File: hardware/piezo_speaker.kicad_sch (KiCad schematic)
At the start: 4 parts, among them Q2 2N3904

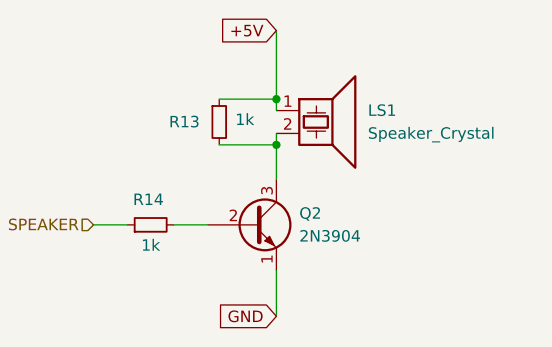
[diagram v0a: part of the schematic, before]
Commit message: Added information, footprints and 3d models for several components
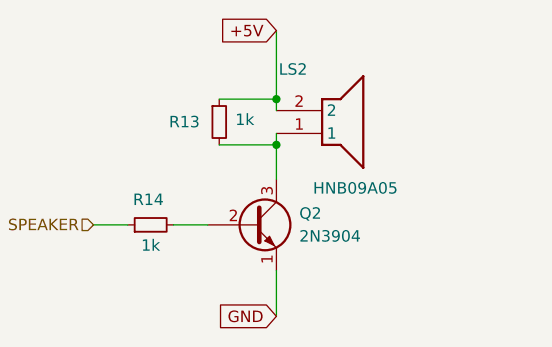
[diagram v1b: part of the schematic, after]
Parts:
- removed LS1: Speaker_Crystal, symbol Device:Speaker_Crystal
- added LS2: HNB09A05, HNB09A05, symbol kitchen_timer-symbols_lib:HNB09A05
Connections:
- net +5V: now also LS2.2
- net at Q2.3 (C), R13.2: now also LS2.1
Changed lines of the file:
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@@
+	)
+	(symbol
+		(lib_id "kitchen_timer-symbols_lib:HNB09A05")
+		(at 148.59 76.2 0)
+		(unit 1)
+		(exclude_from_sim no)
+		(in_bom yes)
+		(on_board yes)
+		(dnp no)
+		(property "Reference" "LS2"
+			(at 148.844 71.628 0)
+			(effects
+				(font
+					(size 1.27 1.27)
+				)
+				(justify left)
+			)
+		)
+		(property "Value" "HNB09A05"
+			(at 152.654 84.836 0)
+			(effects
+				(font
+					(size 1.27 1.27)
+				)
+				(justify left)
+			)
+		)
+		(property "Footprint" "HNB09A05"
+			(at 160.02 178.74 0)
+			(effects
+				(font
+					(size 1.27 1.27)
+				)
+				(justify left top)
+				(hide yes)
+			)
+		)
+		(property "Datasheet" "https://www.lcsc.com/datasheet/lcsc_datasheet_1811141138_Jiangsu-Huaneng-Elec-HNB09A05_C96493.pdf"
+			(at 160.02 278.74 0)
+			(effects
+				(font
+					(size 1.27 1.27)
+				)
+				(justify left top)
+				(hide yes)
+			)
+		)
+		(property "Description" "Buzzers Magnetic YES 3000+/-300Hz 5V 4 ~ 8V 9mm DIP RoHS"
+			(at 150.876 67.056 0)
+			(effects
+				(font
+					(size 1.27 1.27)
+				)
+				(hide yes)
+			)
+		)
+		(property "Height" "5.7"
+			(at 160.02 478.74 0)
+			(effects
+				(font
+					(size 1.27 1.27)
+				)
+				(justify left top)
+				(hide yes)
+			)
+		)
+		(property "Manufacturer_Name" "Jiangsu Huaneng Elec"
+			(at 160.02 578.74 0)
+			(effects
+				(font
+					(size 1.27 1.27)
+				)
+				(justify left top)
+				(hide yes)
+			)
+		)
+		(property "Manufacturer_Part_Number" "HNB09A05"
+			(at 160.02 678.74 0)
+			(effects
+				(font
+					(size 1.27 1.27)
+				)
+				(justify left top)
+				(hide yes)
+			)
+		)
+		(property "Mouser Part Number" ""
+			(at 160.02 778.74 0)
+			(effects
+				(font
+					(size 1.27 1.27)
+				)
+				(justify left top)
+				(hide yes)
+			)
+		)
+		(property "Mouser Price/Stock" ""
+			(at 160.02 878.74 0)
+			(effects
+				(font
+					(size 1.27 1.27)
+				)
+				(justify left top)
+				(hide yes)
+			)
+		)
+		(property "Arrow Part Number" ""
+			(at 160.02 978.74 0)
+			(effects
+				(font
+					(size 1.27 1.27)
+				)
+				(justify left top)
+				(hide yes)
+			)
+		)
+		(property "Arrow Price/Stock" ""
+			(at 160.02 1078.74 0)
+			(effects
+				(font
+					(size 1.27 1.27)
+				)
+				(justify left top)
+				(hide yes)
+			)
+		)
+		(property "Supplier Link" "https://jlcpcb.com/partdetail/Jiangsu_HuanengElec-HNB09A05/C96493"
+			(at 148.59 76.2 0)
+			(effects
+				(font
+					(size 1.27 1.27)
+				)
+				(hide yes)
+			)
+		)
+		(property "Price/unit" "$0.2261"
+			(at 148.59 76.2 0)
+			(effects
+				(font
+					(size 1.27 1.27)
+				)
+				(hide yes)
+			)
+		)
+		(property "Part Num" "HNB09A05"
+			(at 148.59 76.2 0)
+			(effects
+				(font
+					(size 1.27 1.27)
+				)
+				(hide yes)
+			)
+		)
+		(property "Package" "Plugin,D=9mm"
+			(at 148.59 76.2 0)
+			(effects
+				(font
+					(size 1.27 1.27)
+				)
+				(hide yes)
+			)
+		)
+		(pin "2"
+		)
+		(pin "1"
+		)
+		(instances
+			(project ""
+				(path "/8963deea-96bc-4401-b671-98fbe9ed9c6a/cc0cdeb4-aa65-40c1-8591-40f3174b886f"
+					(reference "LS2")
+					(unit 1)
+				)
+			)
+		)
 	)
 	(symbol
@@
 					(unit 1)
 				)
-			)
-		)
-	)
-	(symbol
-		(lib_id "Device:Speaker_Crystal")
-		(at 153.67 76.2 0)
-		(unit 1)
-		(exclude_from_sim no)
-		(in_bom yes)
-		(on_board yes)
-		(dnp no)
-		(fields_autoplaced yes)
-		(property "Reference" "LS1"
-			(at 158.75 76.1999 0)
-			(effects
-				(font
-					(size 1.27 1.27)
-				)
-				(justify left)
-			)
-		)
-		(property "Value" "Speaker_Crystal"
-			(at 158.75 78.7399 0)
-			(effects
-				(font
-					(size 1.27 1.27)
-				)
-				(justify left)
-			)
-		)
-		(property "Footprint" ""
-			(at 152.781 77.47 0)
-			(effects
-				(font
-					(size 1.27 1.27)
-				)
-				(hide yes)
-			)
-		)
-		(property "Datasheet" "~"
-			(at 152.781 77.47 0)
-			(effects
-				(font
-					(size 1.27 1.27)
-				)
-				(hide yes)
-			)
-		)
-		(property "Description" "Crystal speaker/transducer"
-			(at 153.67 76.2 0)
-			(effects
-				(font
-					(size 1.27 1.27)
-				)
-				(hide yes)
-			)
-		)
-		(pin "1"
-		)
-		(pin "2"
-		)
-		(instances
-			(project ""
-				(path "/8963deea-96bc-4401-b671-98fbe9ed9c6a/cc0cdeb4-aa65-40c1-8591-40f3174b886f"
-					(reference "LS1")
-					(unit 1)
-				)

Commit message: Added TP4056 footprint andconfirmed components in UART and BMS schematics.
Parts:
- LS2: footprint HNB09A05 -> kitchen_timer:HNB09A05
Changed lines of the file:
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@@
 			)
 		)
-		(property "Footprint" "HNB09A05"
+		(property "Footprint" "kitchen_timer:HNB09A05"
 			(at 160.02 178.74 0)
 			(effects

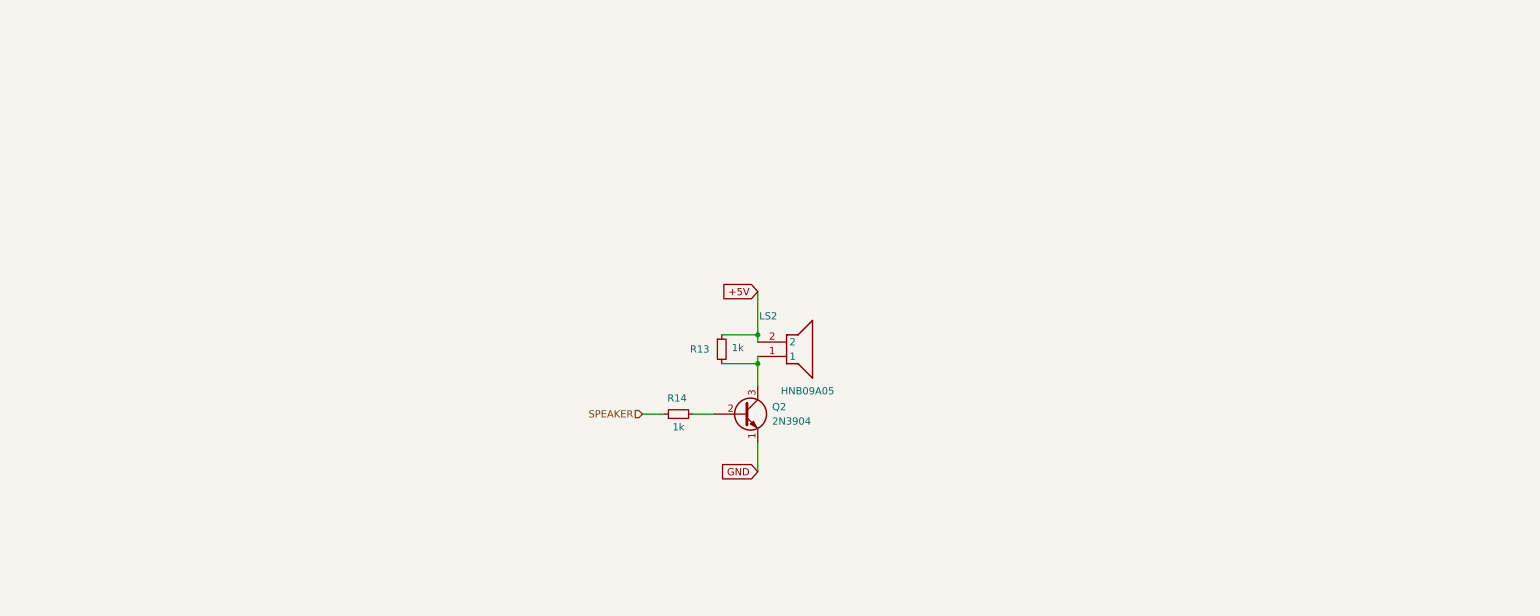
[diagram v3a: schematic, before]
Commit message: Schematic completed, commented and ready for review
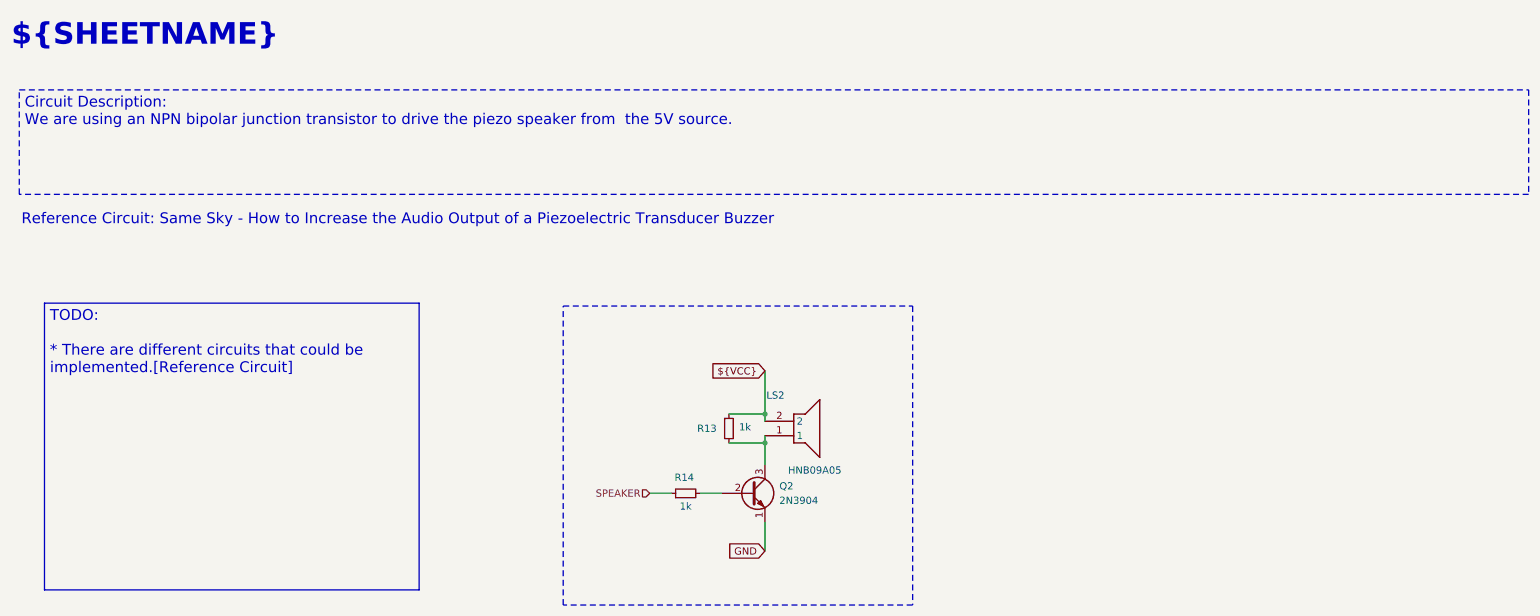
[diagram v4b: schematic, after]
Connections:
- net +5V renamed ${VCC}
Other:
- note added: "${SHEETNAME}"
- note added: "Reference Circuit: Same Sky - How to Increase the Audio Output of a Piezoelectric Transducer Buzzer"
- title: Kitchen_Timer - Piezo Speakr -> Kitchen_Timer - ${SHEETNAME}
- moved on the sheet: LS2, Q2, R13, R14

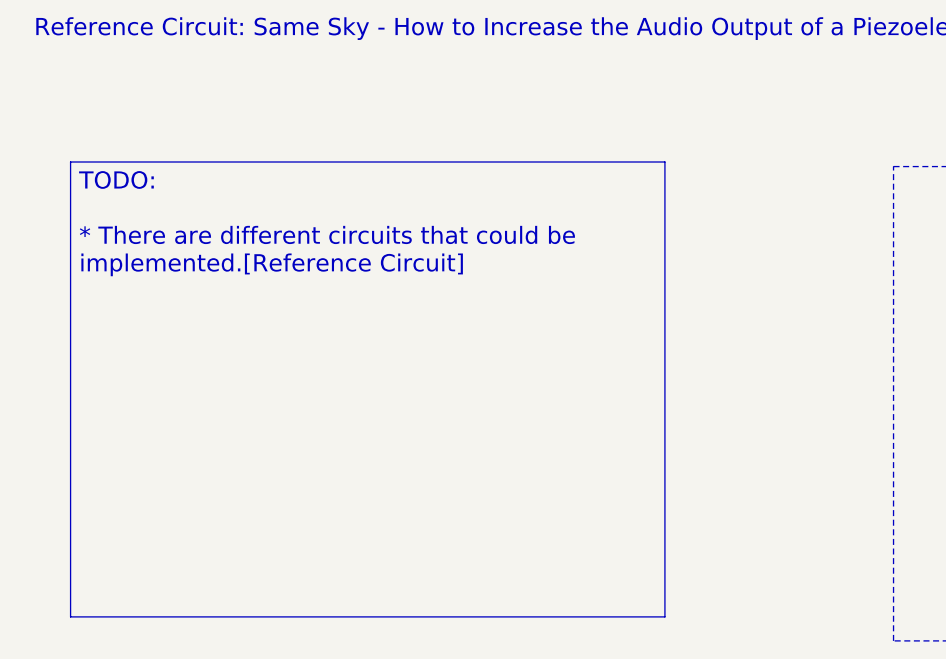
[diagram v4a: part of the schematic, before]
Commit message: Added comments to the TODO boxes after the meeting with Erasmus
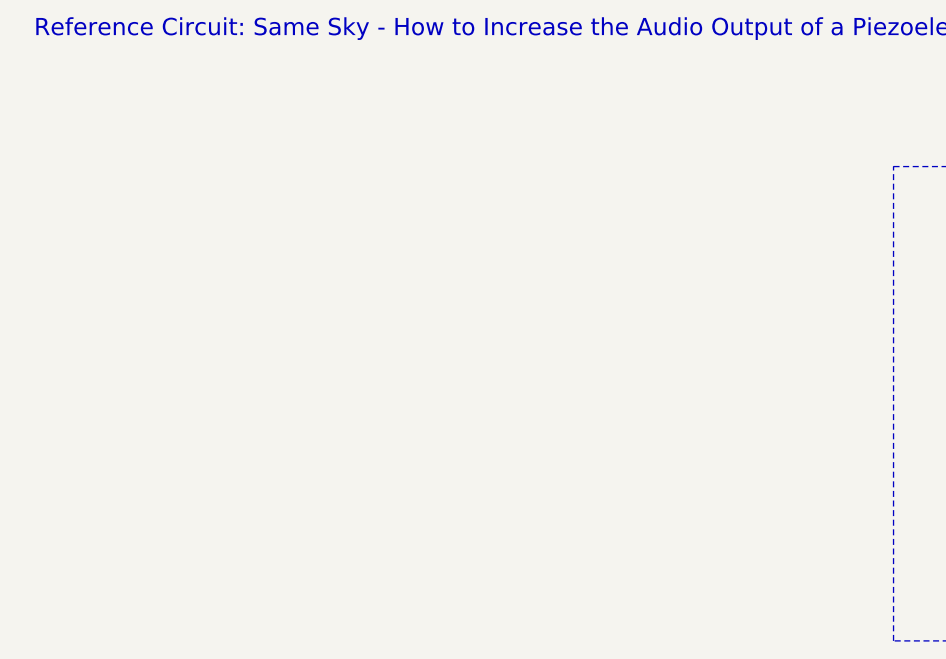
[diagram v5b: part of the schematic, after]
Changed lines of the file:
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@@
-		)
-	)
-	(text_box "TODO:\n\n* There are different circuits that could be implemented.[Reference Circuit]"
-		(exclude_from_sim no)
-		(at 22.86 69.342 0)
-		(size 66.04 50.546)
-		(margins 0.9525 0.9525 0.9525 0.9525)
-		(stroke
-			(width 0)
-			(type solid)
-			(color 194 0 0 1)
-		)
-		(fill
-			(type none)
-		)
-		(effects
-			(font
-				(size 1.905 1.905)
-				(color 194 0 0 1)
-			)
-			(justify left top)
 		)
 	)

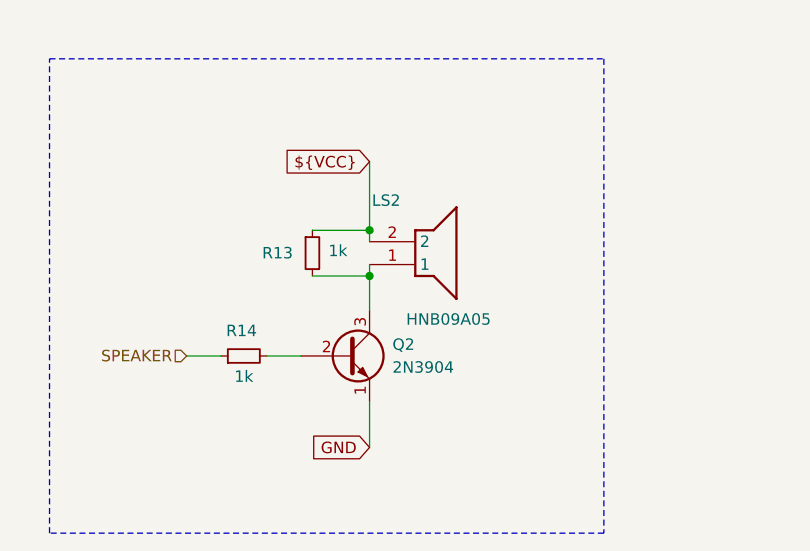
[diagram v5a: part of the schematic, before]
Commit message: Changed from an Active to a Passive buzzer. This will allow us to make tones with a PWM singal
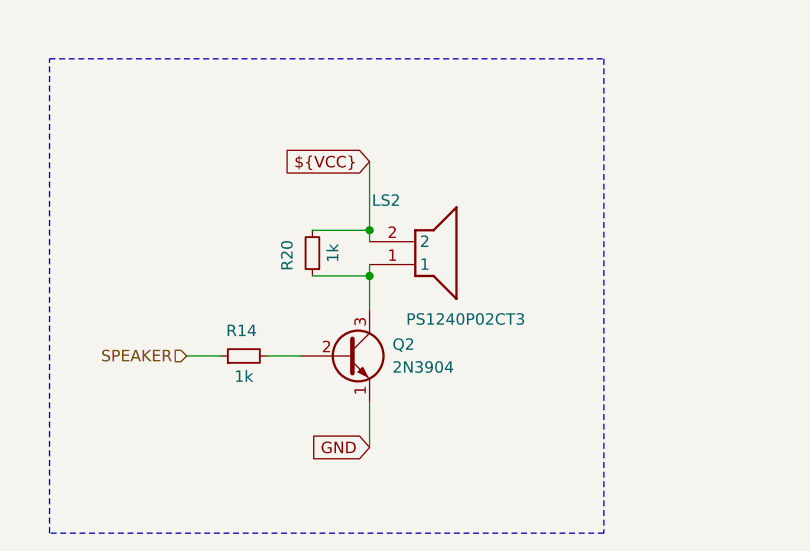
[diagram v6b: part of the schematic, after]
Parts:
- removed R13: 1k, symbol Device:R_Small
- added R20: 1k, symbol Device:R_Small
- LS2: value HNB09A05 -> PS1240P02CT3; footprint kitchen_timer:HNB09A05 -> (none); Height 5.7 -> (none); Manufacturer_Name Jiangsu Huaneng Elec -> TDK; Manufacturer_Part_Number HNB09A05 -> PS1240P02CT3; Package Plugin,D=9mm -> Plugin,D=12.2mm; Part Num HNB09A05 -> C76873; Price/unit $0.2261 -> $0.2409; Supplier Link https://jlcpcb.com/partdetail/Jiangsu_HuanengElec-HNB09A05/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 -> https://jlcpcb.com/partdetail/Tdk-PS1240P02CT3/C76873
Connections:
- net ${VCC}: now also R20.2
- net at LS2.1, Q2.3 (C): now also R20.1
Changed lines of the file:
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@@
+	(wire
+		(pts
+			(xy 149.86 107.95) (xy 149.86 113.03)
+		)
+		(stroke
+			(width 0)
+			(type default)
+		)
+	)
+	(wire
+		(pts
+			(xy 143.51 88.9) (xy 149.86 88.9)
+		)
+		(stroke
+			(width 0)
+			(type default)
+		)
+	)
+	(wire
+		(pts
+			(xy 138.43 102.87) (xy 142.24 102.87)
+		)
+		(stroke
+			(width 0)
+			(type default)
+		)
+	)
+	(wire
+		(pts
+			(xy 149.86 88.9) (xy 149.86 90.17)
+		)
+		(stroke
+			(width 0)
+			(type default)
+		)
+	)
+	(wire
+		(pts
+			(xy 149.86 93.98) (xy 149.86 97.79)
+		)
+		(stroke
+			(width 0)
+			(type default)
+		)
+	)
+	(wire
+		(pts
+			(xy 129.54 102.87) (xy 133.35 102.87)
+		)
+		(stroke
+			(width 0)
+			(type default)
+		)
+	)
+	(wire
+		(pts
+			(xy 143.51 93.98) (xy 149.86 93.98)
+		)
+		(stroke
+			(width 0)
+			(type default)
+		)
+	)
+	(wire
+		(pts
+			(xy 149.86 81.28) (xy 149.86 88.9)
+		)
+		(stroke
+			(width 0)
+			(type default)
+		)
+	)
 	(wire
 		(pts
 			(xy 149.86 92.71) (xy 149.86 93.98)
-		)
-		(stroke
-			(width 0)
-			(type default)
-		)
-	)
-	(wire
-		(pts
-			(xy 149.86 107.95) (xy 149.86 113.03)
-		)
-		(stroke
-			(width 0)
-			(type default)
-		)
-	)
-	(wire
-		(pts
-			(xy 138.43 102.87) (xy 142.24 102.87)
-		)
-		(stroke
-			(width 0)
-			(type default)
-		)
-	)
-	(wire
-		(pts
-			(xy 143.51 93.98) (xy 149.86 93.98)
-		)
-		(stroke
-			(width 0)
-			(type default)
-		)
-	)
-	(wire
-		(pts
-			(xy 129.54 102.87) (xy 133.35 102.87)
-		)
-		(stroke
-			(width 0)
-			(type default)
-		)
-	)
-	(wire
-		(pts
-			(xy 149.86 81.28) (xy 149.86 88.9)
-		)
-		(stroke
-			(width 0)
-			(type default)
-		)
-	)
-	(wire
-		(pts
-			(xy 149.86 88.9) (xy 149.86 90.17)
-		)
-		(stroke
-			(width 0)
-			(type default)
-		)
-	)
-	(wire
-		(pts
-			(xy 143.51 88.9) (xy 149.86 88.9)
-		)
-		(stroke
-			(width 0)
-			(type default)
-		)
-	)
-	(wire
-		(pts
-			(xy 149.86 93.98) (xy 149.86 97.79)
 		)
 		(stroke
@@
 			)
 		)
-		(property "Value" "HNB09A05"
+		(property "Value" "PS1240P02CT3"
 			(at 153.924 98.806 0)
 			(effects
@@
 			)
 		)
-		(property "Footprint" "kitchen_timer:HNB09A05"
+		(property "Footprint" ""
 			(at 161.29 192.71 0)
 			(effects
@@
 			)
 		)
-		(property "Datasheet" "https://www.lcsc.com/datasheet/lcsc_datasheet_1811141138_Jiangsu-Huaneng-Elec-HNB09A05_C96493.pdf"
+		(property "Datasheet" "https://jlcpcb.com/api/file/downloadByFileSystemAccessId/8559368611917037568"
 			(at 161.29 292.71 0)
 			(effects
@@
 			)
 		)
-		(property "Description" "Buzzers Magnetic YES 3000+/-300Hz 5V 4 ~ 8V 9mm DIP RoHS"
+		(property "Description" "Piezo Buzzers & Audio Indicators Round 12.2mmx3.5mm 4kHz Vin=3V"
 			(at 152.146 81.026 0)
 			(effects
@@
 			)
 		)
-		(property "Height" "5.7"
+		(property "Height" ""
 			(at 161.29 492.71 0)
 			(effects
@@
 			)
 		)
-		(property "Manufacturer_Name" "Jiangsu Huaneng Elec"
+		(property "Manufacturer_Name" "TDK"
 			(at 161.29 592.71 0)
 			(effects
@@
 			)
 		)
-		(property "Manufacturer_Part_Number" "HNB09A05"
+		(property "Manufacturer_Part_Number" "PS1240P02CT3"
 			(at 161.29 692.71 0)
 			(effects
@@
 			)
 		)
-		(property "Supplier Link" "https://jlcpcb.com/partdetail/Jiangsu_HuanengElec-HNB09A05/C96493"
+		(property "Supplier Link" "https://jlcpcb.com/partdetail/Tdk-PS1240P02CT3/C76873"
 			(at 149.86 90.17 0)
 			(effects
@@
 			)
 		)
-		(property "Price/unit" "$0.2261"
+		(property "Price/unit" " $0.2409"
 			(at 149.86 90.17 0)
 			(effects
@@
 			)
 		)
-		(property "Part Num" "HNB09A05"
+		(property "Part Num" "C76873"
 			(at 149.86 90.17 0)
 			(effects
@@
 			)
 		)
-		(property "Package" "Plugin,D=9mm"
+		(property "Package" "Plugin,D=12.2mm"
 			(at 149.86 90.17 0)
 			(effects
@@
 				(path "/8963deea-96bc-4401-b671-98fbe9ed9c6a/cc0cdeb4-aa65-40c1-8591-40f3174b886f"
 					(reference "LS2")
+					(unit 1)
+				)
+			)
+		)
+	)
+	(symbol
+		(lib_id "Device:R_Small")
+		(at 143.51 91.44 180)
+		(unit 1)
+		(exclude_from_sim no)
+		(in_bom yes)
+		(on_board yes)
+		(dnp no)
+		(property "Reference" "R20"
+			(at 140.716 91.694 90)
+			(effects
+				(font
+					(size 1.27 1.27)
+				)
+			)
+		)
+		(property "Value" "1k"
+			(at 145.796 91.44 90)
+			(effects
+				(font
+					(size 1.27 1.27)
+				)
+			)
+		)
+		(property "Footprint" ""
+			(at 143.51 91.44 0)
+			(effects
+				(font
+					(size 1.27 1.27)
+				)
+				(hide yes)
+			)
+		)
+		(property "Datasheet" "~"
+			(at 143.51 91.44 0)
+			(effects
+				(font
+					(size 1.27 1.27)
+				)
+				(hide yes)
+			)
+		)
+		(property "Description" "Resistor, small symbol"
+			(at 143.51 91.44 0)
+			(effects
+				(font
+					(size 1.27 1.27)
+				)
+				(hide yes)
+			)
+		)
+		(pin "1"
+		)
+		(pin "2"
+		)
+		(instances
+			(project "kitchen_timer-hardware"
+				(path "/8963deea-96bc-4401-b671-98fbe9ed9c6a/cc0cdeb4-aa65-40c1-8591-40f3174b886f"
+					(reference "R20")
 					(unit 1)
 				)
@@
 					(unit 1)
 				)
-			)
-		)
-	)
-	(symbol
-		(lib_id "Device:R_Small")
-		(at 143.51 91.44 0)
-		(unit 1)
-		(exclude_from_sim no)
-		(in_bom yes)
-		(on_board yes)
-		(dnp no)
-		(property "Reference" "R13"
-			(at 137.922 91.44 0)
-			(effects
-				(font
-					(size 1.27 1.27)
-				)
-				(justify left)
-			)
-		)
-		(property "Value" "1k"
-			(at 145.288 91.186 0)
-			(effects
-				(font
-					(size 1.27 1.27)
-				)
-				(justify left)
-			)
-		)
-		(property "Footprint" ""
-			(at 143.51 91.44 0)
-			(effects
-				(font
-					(size 1.27 1.27)
-				)
-				(hide yes)
-			)
-		)
-		(property "Datasheet" "~"
-			(at 143.51 91.44 0)
-			(effects
-				(font
-					(size 1.27 1.27)
-				)
-				(hide yes)
-			)
-		)
-		(property "Description" "Resistor, small symbol"
-			(at 143.51 91.44 0)
-			(effects
-				(font
-					(size 1.27 1.27)
-				)
-				(hide yes)
-			)
-		)
-		(pin "1"
-		)
-		(pin "2"
-		)
-		(instances
-			(project ""
-				(path "/8963deea-96bc-4401-b671-98fbe9ed9c6a/cc0cdeb4-aa65-40c1-8591-40f3174b886f"
-					(reference "R13")
-					(unit 1)
-				)
